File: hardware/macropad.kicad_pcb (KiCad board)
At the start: 2 copper layers, 63.5 x 106.7 mm, 26 parts, among them J2 Conn_01x06, J3 I2C Screen, J4 SPI Screen, SW1 SW_Push, SW2 SW_Push, SW3 SW_Push, SW4 SW_Push, SW5 SW_Push, SW6 SW_Push, SW7 SW_Push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

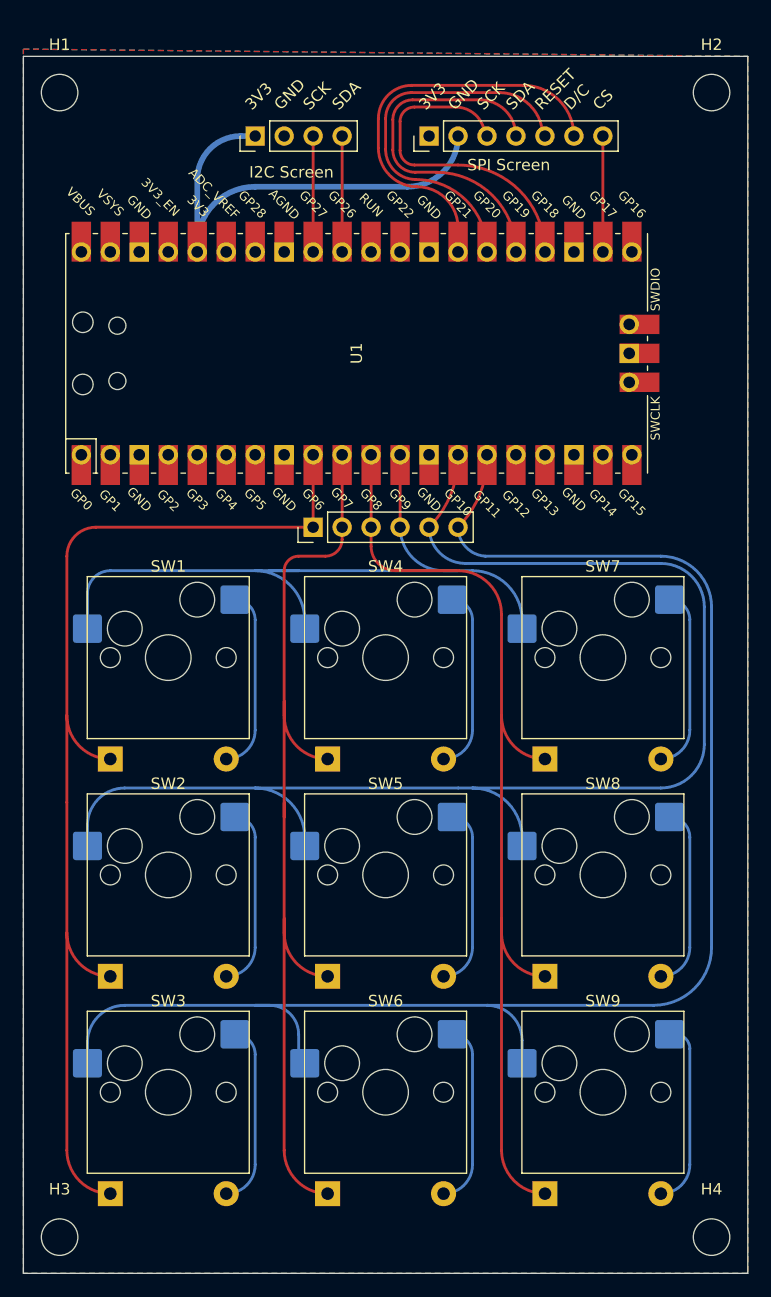
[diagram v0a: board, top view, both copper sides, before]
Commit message: :truck: Test different layout with pi pico in the back
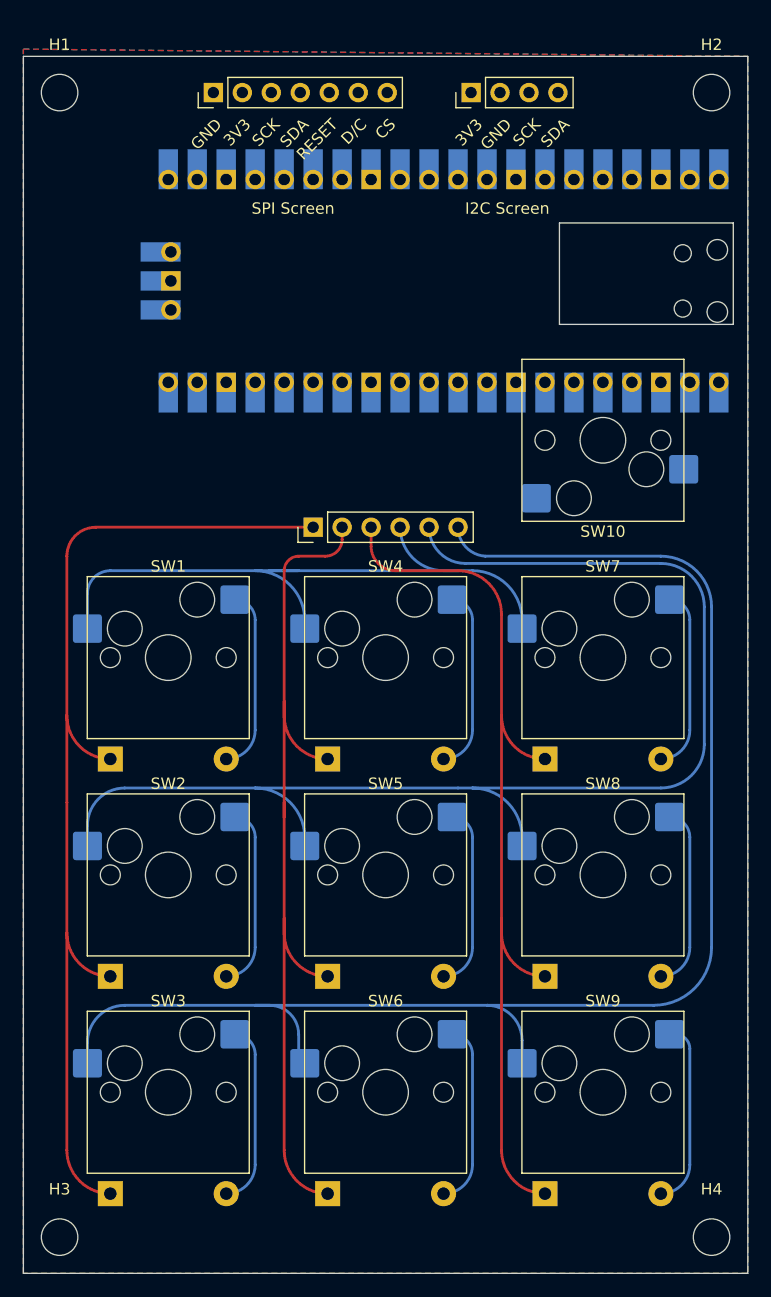
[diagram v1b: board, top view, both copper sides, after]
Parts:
- added SW10: SW_Push, Switch_Keyboard_Hotswap_Kailh:SW_Hotswap_Kailh_MX, F.Cu at (114.3, 57.1)
- U1: moved to B.Cu
- moved J3 19.3 mm to (102.7, 26.7)
- moved J4 19.3 mm to (80.2, 26.7)
- moved U1 9.92 mm to (100.3, 43.2)
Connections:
- J2 pad 1: COL1 -> ROW3
- J2 pad 2: COL2 -> ROW2
- J2 pad 3: COL3 -> ROW1
- J2 pad 4: ROW1 -> COL3
- J2 pad 5: ROW2 -> COL2
- J2 pad 6: ROW3 -> COL1
- U1 pad 1: unconnected-(U1-Pad1) -> ROW0
- U1 pad 10: COL2 -> ROW3
- U1 pad 11: COL3 -> ROW2
- U1 pad 14: ROW2 -> COL3
- U1 pad 15: ROW3 -> COL2
- U1 pad 16: unconnected-(U1-Pad16) -> COL1
- U1 pad 9: COL1 -> COL0
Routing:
- net 3V3: track 42.0 -> 0.00 mm
- net SCREEN_COMMAND: track 36.4 -> 0.00 mm
- net SCREEN_RESET: track 33.6 -> 0.00 mm
- net SPI0_TX: track 31.6 -> 0.00 mm
- net SPI0_SCK: track 29.6 -> 0.00 mm
- net SPI0_CS: track 10.2 -> 0.00 mm
- net SDA: track 10.2 -> 0.00 mm
- net SCK: track 10.2 -> 0.00 mm
- net ROW3: track 138.4 -> 131.4 mm
- net ROW2: track 121.3 -> 114.3 mm
- net ROW1: track 68.7 -> 62.3 mm
- net COL3: track 88.4 -> 82.0 mm
- net COL2: track 86.1 -> 79.7 mm
- net COL1: track 98.9 -> 92.5 mm
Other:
- outline, holes or cut-outs redrawn

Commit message: :construction: Some routing
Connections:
- J2 pad 1: ROW3 -> COL1
- J2 pad 2: ROW2 -> COL2
- J2 pad 3: ROW1 -> COL3
- J2 pad 4: COL3 -> ROW1
- J2 pad 5: COL2 -> ROW2
- J2 pad 6: COL1 -> ROW3
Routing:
- net 3V3: track 0.00 -> 42.2 mm
- net SDA: track 0.00 -> 17.3 mm
- net COL2: track 79.7 -> 93.8 mm
- net COL3: track 82.0 -> 96.1 mm
- net COL1: track 92.5 -> 106.6 mm
- net ROW2: track 114.3 -> 127.0 mm
- net ROW1: track 62.3 -> 75.0 mm
- net ROW3: track 131.4 -> 144.1 mm
- net SCK: track 0.00 -> 9.89 mm
- net SPI0_SCK: track 0.00 -> 8.37 mm
- net SCREEN_COMMAND: track 0.00 -> 8.37 mm
- net SCREEN_RESET: track 0.00 -> 8.37 mm
- net SPI0_TX: track 0.00 -> 8.37 mm
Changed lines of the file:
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@@
       (effects (font (size 1 1) (thickness 0.15)))
     )
-    (fp_text user "${REFERENCE}" (at 0 6.35 180) (layer "F.Fab")
+    (fp_text user "${REFERENCE}" (at 0 6.35) (layer "F.Fab")
       (effects (font (size 1 1) (thickness 0.15)))
     )
@@
     (fp_line (start 1.27 -1.27) (end 1.27 13.97) (layer "F.Fab") (width 0.1))
     (pad "1" thru_hole rect (at 0 0 90) (size 1.7 1.7) (drill 1) (layers *.Cu *.Mask)
-      (net 5 "ROW3") (pinfunction "Pin_1") (pintype "passive"))
+      (net 13 "COL1") (pinfunction "Pin_1") (pintype "passive"))
     (pad "2" thru_hole oval (at 0 2.54 90) (size 1.7 1.7) (drill 1) (layers *.Cu *.Mask)
-      (net 3 "ROW2") (pinfunction "Pin_2") (pintype "passive"))
+      (net 14 "COL2") (pinfunction "Pin_2") (pintype "passive"))
     (pad "3" thru_hole oval (at 0 5.08 90) (size 1.7 1.7) (drill 1) (layers *.Cu *.Mask)
-      (net 1 "ROW1") (pinfunction "Pin_3") (pintype "passive"))
+      (net 15 "COL3") (pinfunction "Pin_3") (pintype "passive"))
     (pad "4" thru_hole oval (at 0 7.62 90) (size 1.7 1.7) (drill 1) (layers *.Cu *.Mask)
-      (net 15 "COL3") (pinfunction "Pin_4") (pintype "passive"))
+      (net 1 "ROW1") (pinfunction "Pin_4") (pintype "passive"))
     (pad "5" thru_hole oval (at 0 10.16 90) (size 1.7 1.7) (drill 1) (layers *.Cu *.Mask)
-      (net 14 "COL2") (pinfunction "Pin_5") (pintype "passive"))
+      (net 3 "ROW2") (pinfunction "Pin_5") (pintype "passive"))
     (pad "6" thru_hole oval (at 0 12.7 90) (size 1.7 1.7) (drill 1) (layers *.Cu *.Mask)
-      (net 13 "COL1") (pinfunction "Pin_6") (pintype "passive"))
+      (net 5 "ROW3") (pinfunction "Pin_6") (pintype "passive"))
     (model "${KICAD6_3DMODEL_DIR}/Connector_PinHeader_2.54mm.3dshapes/PinHeader_1x06_P2.54mm_Vertical.wrl"
       (offset (xyz 0 0 0))
@@
   )
   (segment (start 86.36 68.58) (end 85.09 68.58) (width 0.25) (layer "B.Cu") (net 1))
+  (segment (start 96.52 64.77) (end 96.52 52.07) (width 0.25) (layer "B.Cu") (net 1))
   (segment (start 101.6 68.58) (end 100.33 68.58) (width 0.25) (layer "B.Cu") (net 1))
   (segment (start 102.87 68.58) (end 101.6 68.58) (width 0.25) (layer "B.Cu") (net 1))
@@
   (segment (start 72.39 87.63) (end 83.82 87.63) (width 0.25) (layer "B.Cu") (net 3))
   (segment (start 69.115 92.71) (end 69.115 90.905) (width 0.25) (layer "B.Cu") (net 3))
+  (segment (start 99.06 52.07) (end 99.06 64.77) (width 0.25) (layer "B.Cu") (net 3))
   (segment (start 123.19 83.82) (end 123.19 71.755) (width 0.25) (layer "B.Cu") (net 3))
   (segment (start 102.87 87.63) (end 101.6 87.63) (width 0.25) (layer "B.Cu") (net 3))
@@
   (arc (start 81.28 104.14) (mid 83.076051 103.396051) (end 83.82 101.6) (width 0.25) (layer "B.Cu") (net 4))
   (segment (start 107.215 111.76) (end 107.215 109.755) (width 0.25) (layer "B.Cu") (net 5))
+  (segment (start 101.6 64.77) (end 101.6 52.07) (width 0.25) (layer "B.Cu") (net 5))
   (segment (start 86.36 106.68) (end 83.82 106.68) (width 0.25) (layer "B.Cu") (net 5))
   (segment (start 72.39 106.68) (end 83.82 106.68) (width 0.25) (layer "B.Cu") (net 5))
@@
   (arc (start 67.31 67.31) (mid 68.053949 65.513949) (end 69.85 64.77) (width 0.25) (layer "F.Cu") (net 13))
   (arc (start 67.31 119.380004) (mid 68.425922 122.074078) (end 71.12 123.19) (width 0.25) (layer "F.Cu") (net 13))
+  (segment (start 86.36 62.23) (end 86.36 52.07) (width 0.25) (layer "B.Cu") (net 13))
+  (arc (start 88.9 64.77) (mid 87.103949 64.026051) (end 86.36 62.23) (width 0.25) (layer "B.Cu") (net 13))
   (segment (start 86.36 88.9) (end 86.36 90.17) (width 0.25) (layer "F.Cu") (net 14))
   (segment (start 87.63 67.31) (end 89.97056 67.31) (width 0.25) (layer "F.Cu") (net 14))
@@
   (arc (start 89.97056 67.31) (mid 91.009611 66.879611) (end 91.44 65.84056) (width 0.25) (layer "F.Cu") (net 14))
   (arc (start 90.17 104.14) (mid 87.475923 103.024077) (end 86.36 100.33) (width 0.25) (layer "F.Cu") (net 14))
+  (segment (start 88.9 52.07) (end 88.9 57.15) (width 0.25) (layer "B.Cu") (net 14))
+  (segment (start 91.44 59.69) (end 91.44 64.77) (width 0.25) (layer "B.Cu") (net 14))
+  (arc (start 90.17 58.42) (mid 91.068026 58.791974) (end 91.44 59.69) (width 0.25) (layer "B.Cu") (net 14))
+  (arc (start 88.9 57.15) (mid 89.271974 58.048026) (end 90.17 58.42) (width 0.25) (layer "B.Cu") (net 14))
   (segment (start 105.41 100.33) (end 105.41 99.06) (width 0.25) (layer "F.Cu") (net 15))
   (segment (start 101.6 68.58) (end 96.11425 68.58) (width 0.25) (layer "F.Cu") (net 15))
@@
   (arc (start 96.11425 68.58) (mid 94.605107 67.954893) (end 93.98 66.44575) (width 0.25) (layer "F.Cu") (net 15))
   (arc (start 109.22 85.09) (mid 106.525923 83.974077) (end 105.41 81.28) (width 0.25) (layer "F.Cu") (net 15))
+  (segment (start 91.44 52.07) (end 91.44 57.15) (width 0.25) (layer "B.Cu") (net 15))
+  (segment (start 93.98 59.69) (end 93.98 64.77) (width 0.25) (layer "B.Cu") (net 15))
+  (arc (start 92.71 58.42) (mid 93.608026 58.791974) (end 93.98 59.69) (width 0.25) (layer "B.Cu") (net 15))
+  (arc (start 91.44 57.15) (mid 91.811974 58.048026) (end 92.71 58.42) (width 0.25) (layer "B.Cu") (net 15))
+  (segment (start 106.045 30.353) (end 105.380608 30.353) (width 0.25) (layer "B.Cu") (net 17))
+  (segment (start 104.14 34.29) (end 104.14 31.593608) (width 0.25) (layer "B.Cu") (net 17))
+  (segment (start 107.82103 28.57697) (end 107.82103 26.67) (width 0.25) (layer "B.Cu") (net 17))
+  (arc (start 106.045 30.353) (mid 107.300843 29.832813) (end 107.82103 28.57697) (width 0.25) (layer "B.Cu") (net 17))
+  (arc (start 104.14 31.593608) (mid 104.503366 30.716366) (end 105.380608 30.353) (width 0.25) (layer "B.Cu") (net 17))
+  (segment (start 108.58303 24.892) (end 107.747042 24.892) (width 0.25) (layer "B.Cu") (net 18))
+  (segment (start 106.553 26.086042) (end 106.553 28.432663) (width 0.25) (layer "B.Cu") (net 18))
+  (segment (start 105.267663 29.718) (end 103.053719 29.718) (width 0.25) (layer "B.Cu") (net 18))
+  (segment (start 101.6 31.171719) (end 101.6 34.29) (width 0.25) (layer "B.Cu") (net 18))
+  (arc (start 110.36103 26.67) (mid 109.840266 25.412764) (end 108.58303 24.892) (width 0.25) (layer "B.Cu") (net 18))
+  (arc (start 107.747042 24.892) (mid 106.902727 25.241727) (end 106.553 26.086042) (width 0.25) (layer "B.Cu") (net 18))
+  (arc (start 106.553 28.432663) (mid 106.176534 29.341534) (end 105.267663 29.718) (width 0.25) (layer "B.Cu") (net 18))
+  (arc (start 103.053719 29.718) (mid 102.025784 30.143784) (end 101.6 31.171719) (width 0.25) (layer "B.Cu") (net 18))
+  (segment (start 106.299 29.337) (end 112.116231 29.337) (width 0.5) (layer "F.Cu") (net 20))
+  (segment (start 106.299 29.337) (end 105.40803 29.337) (width 0.5) (layer "F.Cu") (net 20))
+  (segment (start 114.3 34.29) (end 114.3 31.520769) (width 0.5) (layer "F.Cu") (net 20))
+  (segment (start 84.691049 29.337) (end 106.299 29.337) (width 0.5) (layer "F.Cu") (net 20))
+  (segment (start 82.6925 26.67) (end 82.6925 27.338451) (width 0.5) (layer "F.Cu") (net 20))
+  (arc (start 112.116231 29.337) (mid 113.660389 29.976611) (end 114.3 31.520769) (width 0.5) (layer "F.Cu") (net 20))
+  (arc (start 82.6925 27.338451) (mid 83.277861 28.751639) (end 84.691049 29.337) (width 0.5) (layer "F.Cu") (net 20))
+  (arc (start 105.40803 29.337) (mid 103.522176 28.555854) (end 102.74103 26.67) (width 0.5) (layer "F.Cu") (net 20))
+  (segment (start 83.82 28.0825) (end 83.82 34.29) (width 0.25) (layer "B.Cu") (net 27))
+  (arc (start 85.2325 26.67) (mid 84.233712 27.083712) (end 83.82 28.0825) (width 0.25) (layer "B.Cu") (net 27))
+  (segment (start 86.36 28.0825) (end 86.36 34.29) (width 0.25) (layer "B.Cu") (net 30))
+  (arc (start 87.7725 26.67) (mid 86.773712 27.083712) (end 86.36 28.0825) (width 0.25) (layer "B.Cu") (net 30))
+  (segment (start 88.9 28.0825) (end 88.9 34.29) (width 0.25) (layer "B.Cu") (net 31))
+  (arc (start 90.3125 26.67) (mid 89.313712 27.083712) (end 88.9 28.0825) (width 0.25) (layer "B.Cu") (net 31))
+  (segment (start 91.44 28.0825) (end 91.44 34.29) (width 0.25) (layer "B.Cu") (net 32))
+  (arc (start 92.8525 26.67) (mid 91.853712 27.083712) (end 91.44 28.0825) (width 0.25) (layer "B.Cu") (net 32))
   (zone (net 16) (net_name "GND") (layers F&B.Cu) (hatch edge 0.508)
     (connect_pads (clearance 0.508))
     (min_thickness 0.254) (filled_areas_thickness no)
-    (fill (thermal_gap 0.508) (thermal_bridge_width 0.508))
+    (fill yes (thermal_gap 0.508) (thermal_bridge_width 0.508))
     (polygon
       (pts

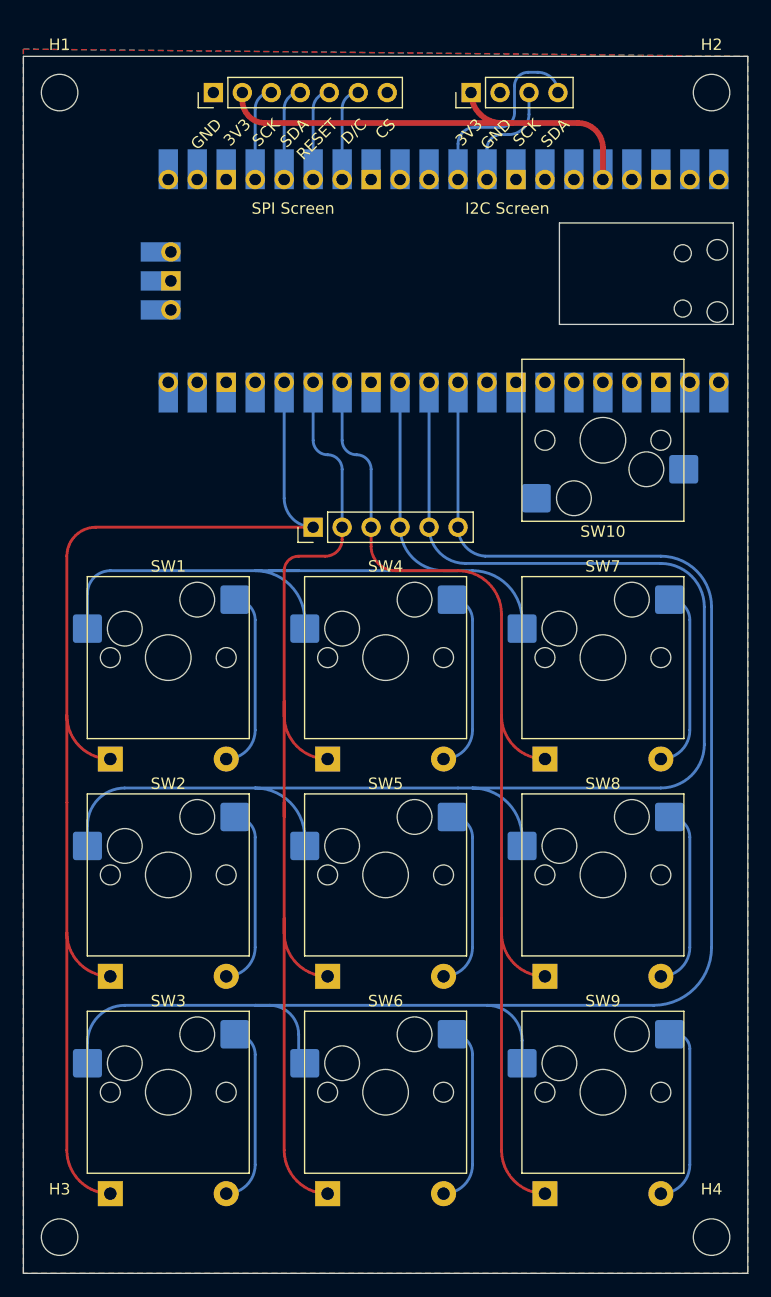
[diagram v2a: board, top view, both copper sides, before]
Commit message: :construction: Edit pi pico to remove tht pads & add castellated pads for D+/D-
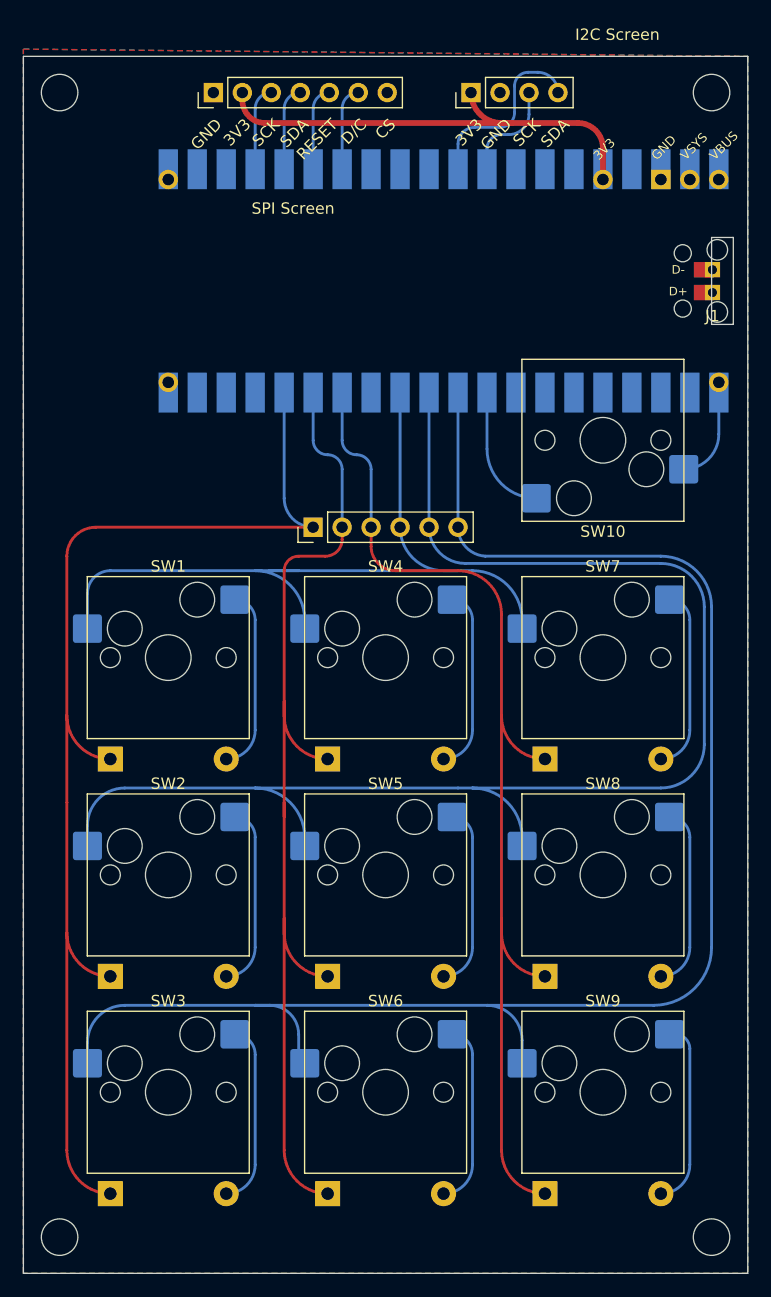
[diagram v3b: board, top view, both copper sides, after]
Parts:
- added J1: Conn_01x02, Connector_PinHeader_2.00mm:PinHeader_1x02_P2.00mm_Vertical, F.Cu at (123.9, 44.2)
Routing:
- net COL0: track 0.00 -> 12.5 mm
- net ROW0: track 0.00 -> 9.25 mm
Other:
- outline, holes or cut-outs redrawn
- board text added: "D+"
- board text added: "D-"
- board text added: "VBUS"
- board text added: "VSYS"
